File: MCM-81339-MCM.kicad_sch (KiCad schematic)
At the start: 35 parts, among them J3 Conn_02x03_Odd_Even, J5 USB_B_Mini, U5 ESP32-S3-WROOM-2

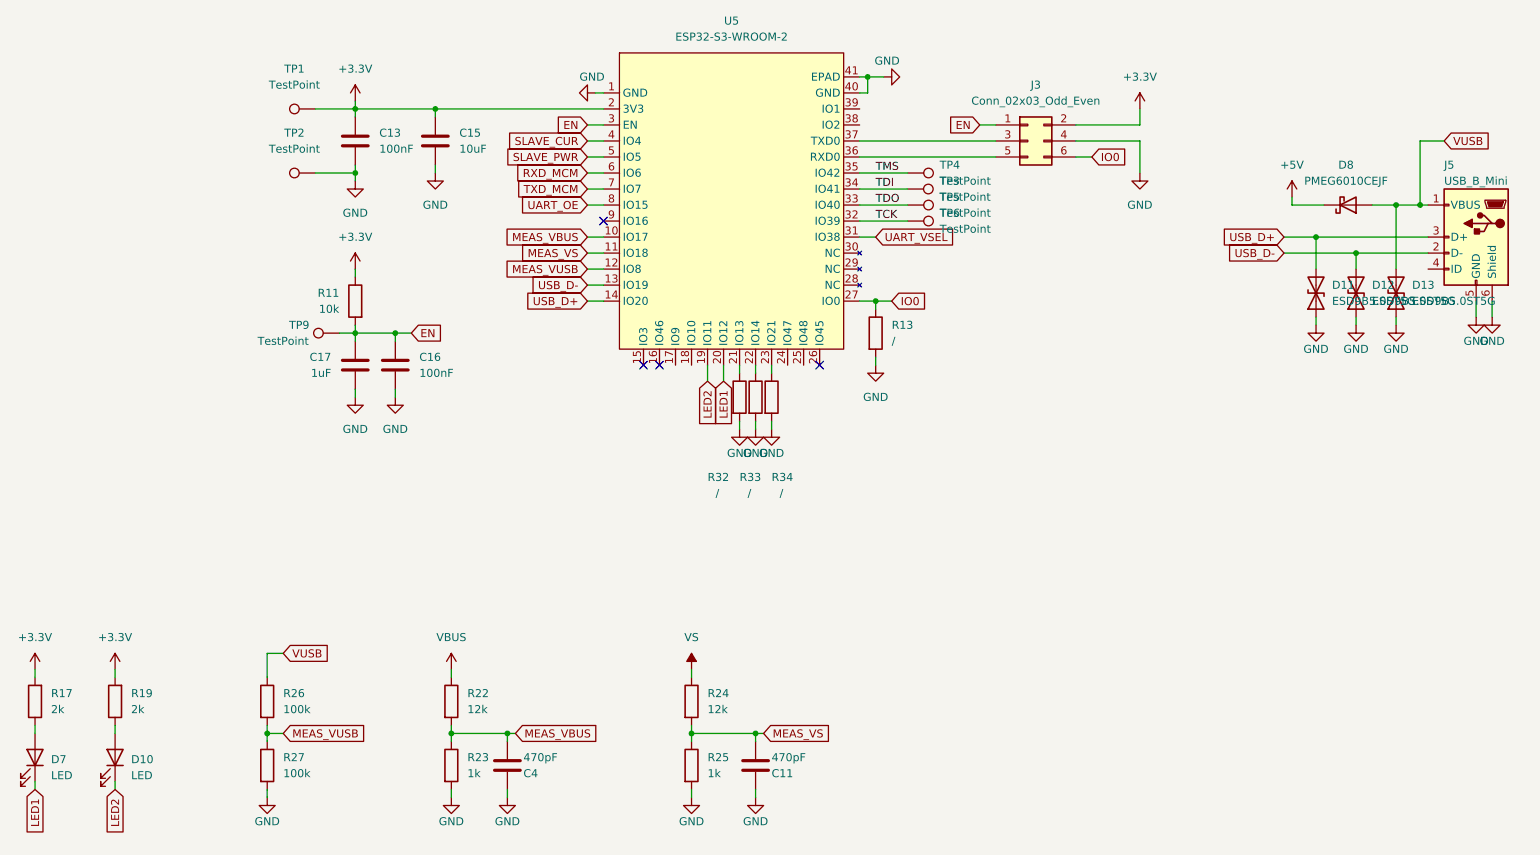
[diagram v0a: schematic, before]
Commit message: add protection on uart, add fab outputs
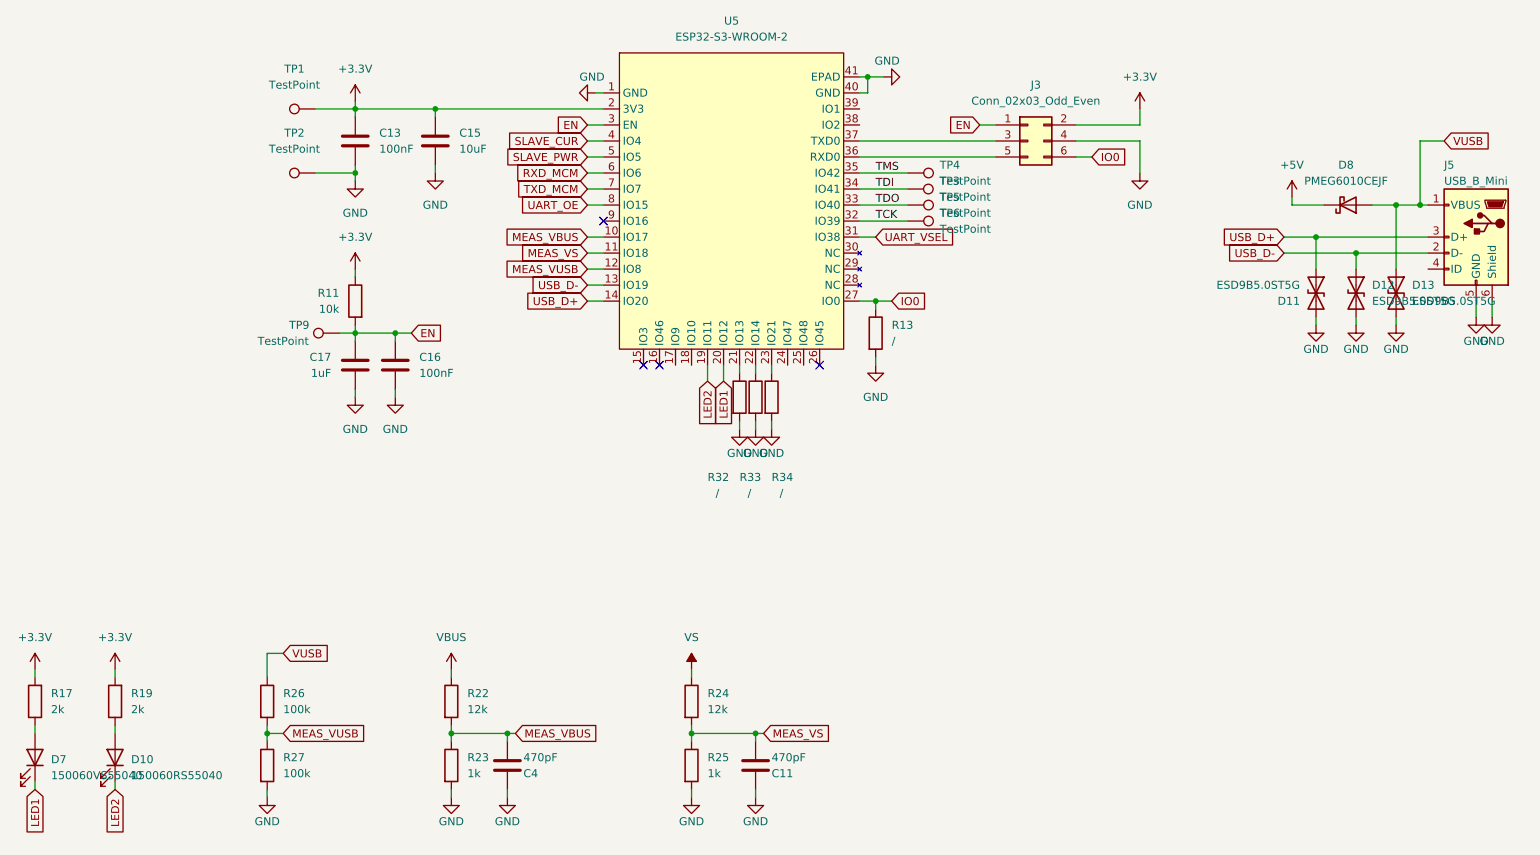
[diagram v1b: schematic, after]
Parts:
- D10: value LED -> 150060RS55040
- D7: value LED -> 150060VS55040
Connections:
- net GND: now also D11.2 (A2), D12.2 (A2), D13.2 (A2); no longer D11.1 (A1), D12.1 (A1), D13.1 (A1)
- net USB_D+: now also D11.1 (A1); no longer D11.2 (A2)
- net USB_D-: now also D12.1 (A1); no longer D12.2 (A2)
- net VUSB: now also D13.1 (A1); no longer D13.2 (A2)
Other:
- moved on the sheet: D11, D12, D13

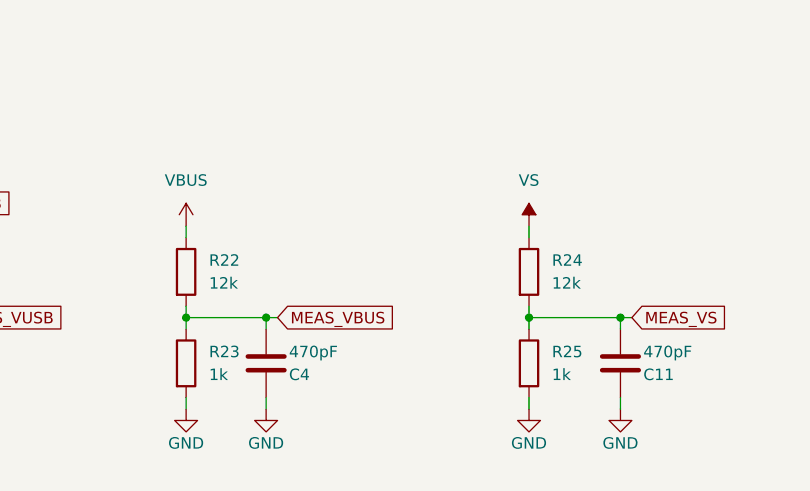
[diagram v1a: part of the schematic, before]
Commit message: R22/R24 to 9k09 for more resolution
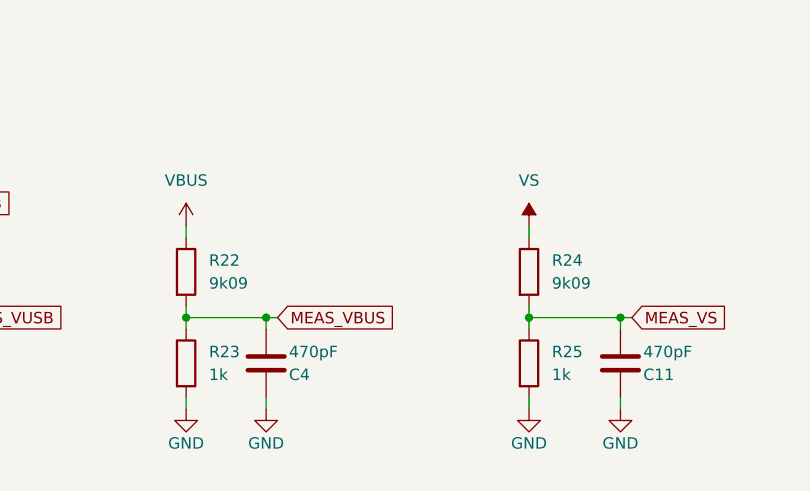
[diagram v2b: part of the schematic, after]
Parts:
- R22, R24: value 12k -> 9k09
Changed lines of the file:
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@@
       (effects (font (size 1.27 1.27)) (justify left))
     )
-    (property "Value" "12k" (id 1) (at 139.7 161.2899 0)
+    (property "Value" "9k09" (id 1) (at 139.7 161.2899 0)
       (effects (font (size 1.27 1.27)) (justify left))
     )
@@
       (effects (font (size 1.27 1.27)) (justify left))
     )
-    (property "Value" "12k" (id 1) (at 101.6 161.2899 0)
+    (property "Value" "9k09" (id 1) (at 101.6 161.2899 0)
       (effects (font (size 1.27 1.27)) (justify left))
     )

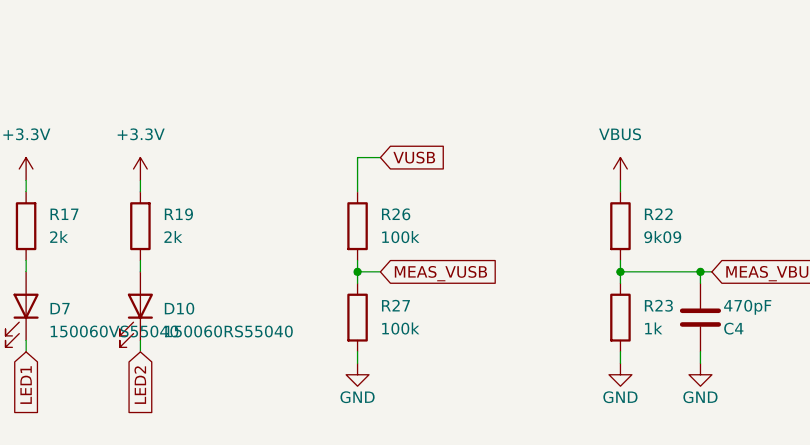
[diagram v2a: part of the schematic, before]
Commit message: update vusb monitor voltage divider
updating vusb voltage divider to get inline with https://docs.espressif.com/projects/esp-idf/en/release-v5.1/esp32s3/api-reference/peripherals/usb_device.html#self-powered-device
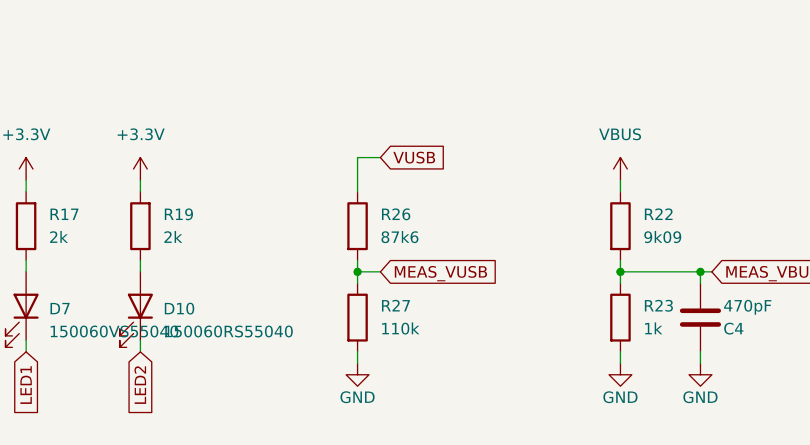
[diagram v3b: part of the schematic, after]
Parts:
- R26: value 100k -> 87k6
- R27: value 100k -> 110k
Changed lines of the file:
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@@
       (effects (font (size 1.27 1.27)) (justify left))
     )
-    (property "Value" "100k" (id 1) (at 72.39 171.4499 0)
+    (property "Value" "110k" (id 1) (at 72.39 171.4499 0)
       (effects (font (size 1.27 1.27)) (justify left))
     )
@@
       (effects (font (size 1.27 1.27)) (justify left))
     )
-    (property "Value" "100k" (id 1) (at 72.39 161.2899 0)
+    (property "Value" "87k6" (id 1) (at 72.39 161.2899 0)
       (effects (font (size 1.27 1.27)) (justify left))
     )
@@
     (pin "1")
   )
+  (sheet_instances
+    (path "/" (page "1"))
+  )
+  (symbol_instances
+    (path "/a512da26-90b0-4ad1-b414-4f5b636f585d"
+      (reference "#PWR01") (unit 1) (value "GND") (footprint "")
+    )
+    (path "/07a4265d-3743-464c-84a0-bda5a34dff7e"
+      (reference "#PWR0130") (unit 1) (value "GND") (footprint "")
+    )
+    (path "/ff3fce4b-50c1-47c2-82ec-c8ec7323b658"
+      (reference "#PWR0131") (unit 1) (value "GND") (footprint "")
+    )
+    (path "/ec2a53fb-5034-4047-8925-cf00391e0117"
+      (reference "#PWR0132") (unit 1) (value "+5V") (footprint "")
+    )
+    (path "/0f37fff6-0fcd-43ec-b64a-f3a6f9cd0d4b"
+      (reference "#PWR0133") (unit 1) (value "GND") (footprint "")
+    )
+    (path "/432211a4-e1f5-498e-969b-56b73638dc5d"
+      (reference "#PWR0134") (unit 1) (value "GND") (footprint "")
+    )
+    (path "/588f378a-ad89-4361-8a6a-c854296bbc92"
+      (reference "#PWR0135") (unit 1) (value "+3.3V") (footprint "")
+    )
+    (path "/6beaa5bd-15ad-4ca4-8935-98a262565292"
+      (reference "#PWR0136") (unit 1) (value "GND") (footprint "")
+    )
+    (path "/728547ca-0b6c-4bab-a1f8-ce21ba9eea66"
+      (reference "#PWR0137") (unit 1) (value "GND") (footprint "")
+    )
+    (path "/7fb277b9-ddb7-4235-894a-7396bcac4ffd"
+      (reference "#PWR0138") (unit 1) (value "+3.3V") (footprint "")
+    )
+    (path "/4e32cc18-1f61-4970-83c3-f8616a2b9f23"
+      (reference "#PWR0139") (unit 1) (value "+3.3V") (footprint "")
+    )
+    (path "/1fadbdd2-16e5-48d6-a35c-2ce721a862e6"
+      (reference "#PWR0140") (unit 1) (value "GND") (footprint "")
+    )
+    (path "/fe850a22-a98d-4d57-9b15-b062912256ed"
+      (reference "#PWR0141") (unit 1) (value "+3.3V") (footprint "")
+    )
+    (path "/6991c44c-e555-42e2-9a9b-08077ea46525"
+      (reference "#PWR0142") (unit 1) (value "GND") (footprint "")
+    )
+    (path "/de0bf633-e9ed-4c7b-a718-e38608204adf"
+      (reference "#PWR0143") (unit 1) (value "GND") (footprint "")
+    )
+    (path "/6c9206fb-eaa0-4897-9024-722230e14d0c"
+      (reference "#PWR0144") (unit 1) (value "+3.3V") (footprint "")
+    )
+    (path "/fe86d367-24e1-43ff-8e0f-5dd999f6717f"
+      (reference "#PWR0145") (unit 1) (value "GND") (footprint "")
+    )
+    (path "/5bccc591-d8c9-4e2e-a1c5-0ad5cafc8380"
+      (reference "#PWR0146") (unit 1) (value "VBUS") (footprint "")
+    )
+    (path "/660f3b83-d37a-4d03-ba2f-abbc4db2de7b"
+      (reference "#PWR0147") (unit 1) (value "GND") (footprint "")
+    )
+    (path "/a89de7a5-c8a0-4697-a76a-8c0a74e23084"
+      (reference "#PWR0148") (unit 1) (value "GND") (footprint "")
+    )
+    (path "/ad614bc0-4d2f-45cc-844b-78fcf25372a1"
+      (reference "#PWR0149") (unit 1) (value "VS") (footprint "")
+    )
+    (path "/cda16e13-e43d-487b-a300-7880bfc03708"
+      (reference "#PWR0150") (unit 1) (value "GND") (footprint "")
+    )
+    (path "/967042b5-4b7a-4c98-a5e8-7efca0b65054"
+      (reference "#PWR0151") (unit 1) (value "GND") (footprint "")
+    )
+    (path "/edc0ee2d-715b-4072-afa2-6cda4d946601"
+      (reference "#PWR0152") (unit 1) (value "GND") (footprint "")
+    )
+    (path "/a611f0d0-59b9-45ae-a121-327fa3788fcb"
+      (reference "#PWR0153") (unit 1) (value "GND") (footprint "")
+    )
+    (path "/3b091975-5427-40db-a3e2-8a25295ebd62"
+      (reference "#PWR0154") (unit 1) (value "GND") (footprint "")
+    )
+    (path "/9feea155-d22d-482d-8bf7-57309a8c16e0"
+      (reference "#PWR0155") (unit 1) (value "GND") (footprint "")
+    )
+    (path "/0395221b-7de6-4cfa-90be-4e99f7c4919e"
+      (reference "#PWR0156") (unit 1) (value "GND") (footprint "")
+    )
+    (path "/bb41d442-d871-48d8-a62c-00607a03e30c"
+      (reference "#PWR0157") (unit 1) (value "GND") (footprint "")
+    )
+    (path "/9e9ae0a4-ec6c-4398-bc24-ad0b433f657c"
+      (reference "C4") (unit 1) (value "470pF") (footprint "Capacitor_SMD:C_0402_1005Metric")
+    )
+    (path "/d545b7e7-927c-4bff-a3ee-bcaec2830f9e"
+      (reference "C11") (unit 1) (value "470pF") (footprint "Capacitor_SMD:C_0402_1005Metric")
+    )
+    (path "/96bdf7e2-fc5f-4bd3-8858-cbb210e0280c"
+      (reference "C13") (unit 1) (value "100nF") (footprint "Capacitor_SMD:C_0402_1005Metric")
+    )
+    (path "/b8721f84-b8d2-4bef-8177-c35bdbd198c0"
+      (reference "C15") (unit 1) (value "10uF") (footprint "Capacitor_SMD:C_1206_3216Metric")
+    )
+    (path "/671a430f-fa11-4bd3-9146-21044a2e710f"
+      (reference "C16") (unit 1) (value "100nF") (footprint "Capacitor_SMD:C_0402_1005Metric")
+    )
+    (path "/85383b02-f665-4bdb-8d30-24ac663a701c"
+      (reference "C17") (unit 1) (value "1uF") (footprint "Capacitor_SMD:C_0402_1005Metric")
+    )
+    (path "/2e5d5d6d-66e5-480c-9d70-d3c142363262"
+      (reference "D7") (unit 1) (value "150060VS55040") (footprint "LED_SMD:LED_0603_1608Metric")
+    )
+    (path "/8345625a-2806-457d-89f5-d8c4b2c12e0f"
+      (reference "D8") (unit 1) (value "PMEG6010CEJF") (footprint "Diode_SMD:D_SOD-323F")
+    )
+    (path "/42fff36f-bacf-4bdf-a68a-1203b70d1064"
+      (reference "D10") (unit 1) (value "150060RS55040") (footprint "LED_SMD:LED_0603_1608Metric")
+    )
+    (path "/990b8ae3-c48c-4659-a142-5c4eb282fb7e"
+      (reference "D11") (unit 1) (value "ESD9B5.0ST5G") (footprint "Diode_SMD:D_SOD-923")
+    )
+    (path "/4efe8f4c-960b-4b4c-b38f-b167b569996e"
+      (reference "D12") (unit 1) (value "ESD9B5.0ST5G") (footprint "Diode_SMD:D_SOD-923")
+    )
+    (path "/7ff5746b-238f-4742-829b-41ca77de7a92"
+      (reference "D13") (unit 1) (value "ESD9B5.0ST5G") (footprint "Diode_SMD:D_SOD-923")
+    )
+    (path "/121686ee-d63e-4f46-b1be-7c3847d981ae"
+      (reference "J3") (unit 1) (value "Conn_02x03_Odd_Even") (footprint "Connector_PinHeader_2.00mm:PinHeader_1x06_P2.00mm_Vertical")
+    )
+    (path "/b16446e8-c716-4508-ac33-6b11e18fa5b2"
+      (reference "J5") (unit 1) (value "USB_B_Mini") (footprint "Connector_USB:USB_Mini-B_Wuerth_65100516121_Horizontal")
+    )
+    (path "/ed070f42-02f9-484f-9141-d09d012dc640"
+      (reference "R11") (unit 1) (value "10k") (footprint "Resistor_SMD:R_0402_1005Metric")
+    )
+    (path "/c123767f-bf20-4e1e-85ce-e10a4bfb3ebe"
+      (reference "R13") (unit 1) (value "/") (footprint "Resistor_SMD:R_0402_1005Metric")
+    )
+    (path "/87df298f-1c8a-49b1-b11f-75bd3967a21b"
+      (reference "R17") (unit 1) (value "2k") (footprint "Resistor_SMD:R_0603_1608Metric")
+    )
+    (path "/57c6c356-e710-48ef-b0b7-fe13fede5acf"
+      (reference "R19") (unit 1) (value "2k") (footprint "Resistor_SMD:R_0603_1608Metric")
+    )
+    (path "/ed7247bd-faeb-4310-9fda-cf37c6b420db"
+      (reference "R22") (unit 1) (value "9k09") (footprint "Resistor_SMD:R_0402_1005Metric")
+    )
+    (path "/d1207b5e-d763-45cd-8fd8-735bcf77ac39"
+      (reference "R23") (unit 1) (value "1k") (footprint "Resistor_SMD:R_0402_1005Metric")
+    )
+    (path "/d225eecb-4d2d-4ebc-bc65-a80f97d891cf"
+      (reference "R24") (unit 1) (value "9k09") (footprint "Resistor_SMD:R_0402_1005Metric")
+    )
+    (path "/94ce5aa1-2dea-40fa-98ce-c2ad0a8a6941"
+      (reference "R25") (unit 1) (value "1k") (footprint "Resistor_SMD:R_0402_1005Metric")
+    )
+    (path "/8cdb8189-4f1a-4c3d-901f-28e5efbf1759"
+      (reference "R26") (unit 1) (value "87k6") (footprint "Resistor_SMD:R_0402_1005Metric")
+    )
+    (path "/2a29fd95-6713-4e44-a108-ed8b91050f57"
+      (reference "R27") (unit 1) (value "110k") (footprint "Resistor_SMD:R_0402_1005Metric")
+    )
+    (path "/ca519420-48db-4eb8-b286-14d6af3b7afd"
+      (reference "R32") (unit 1) (value "/") (footprint "Resistor_SMD:R_0402_1005Metric")
+    )
+    (path "/75c1c33c-38a2-4d9a-9cd0-d1c41eaa0048"
+      (reference "R33") (unit 1) (value "/") (footprint "Resistor_SMD:R_0402_1005Metric")
+    )
+    (path "/db46357a-2240-4019-addb-8038c1793978"
+      (reference "R34") (unit 1) (value "/") (footprint "Resistor_SMD:R_0402_1005Metric")
+    )
+    (path "/6b0c4b71-12b6-4e24-86dd-96d8f7977a05"
+      (reference "TP1") (unit 1) (value "TestPoint") (footprint "TestPoint:TestPoint_Pad_D1.5mm")
+    )
+    (path "/b06610f7-9365-4a5c-abb4-e73298a89c85"
+      (reference "TP2") (unit 1) (value "TestPoint") (footprint "TestPoint:TestPoint_Pad_D1.5mm")
+    )
+    (path "/4b872690-f62c-439c-99d0-8f06392491fc"
+      (reference "TP3") (unit 1) (value "TestPoint") (footprint "TestPoint:TestPoint_Pad_D1.0mm")
+    )
+    (path "/620bb756-65bd-4587-a6f1-0f9aff4bcf5c"
+      (reference "TP4") (unit 1) (value "TestPoint") (footprint "TestPoint:TestPoint_Pad_D1.0mm")
+    )
+    (path "/bbda2527-1e4f-460a-9bea-fb916d574c0e"
+      (reference "TP5") (unit 1) (value "TestPoint") (footprint "TestPoint:TestPoint_Pad_D1.0mm")
+    )
+    (path "/405a1a4f-4845-4340-b7a0-ee4fdc54cf37"
+      (reference "TP6") (unit 1) (value "TestPoint") (footprint "TestPoint:TestPoint_Pad_D1.0mm")
+    )
+    (path "/b59d1dae-f046-4260-abd0-a9a4fe603bfb"
+      (reference "TP9") (unit 1) (value "TestPoint") (footprint "TestPoint:TestPoint_Pad_D1.0mm")
+    )
+    (path "/92da35eb-cd31-4391-be78-b00407543c2b"
+      (reference "U5") (unit 1) (value "ESP32-S3-WROOM-2") (footprint "Melexis:ESP32-S3-WROOM-2")
+    )
+  )
 )

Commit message: use nc pins to route gnd
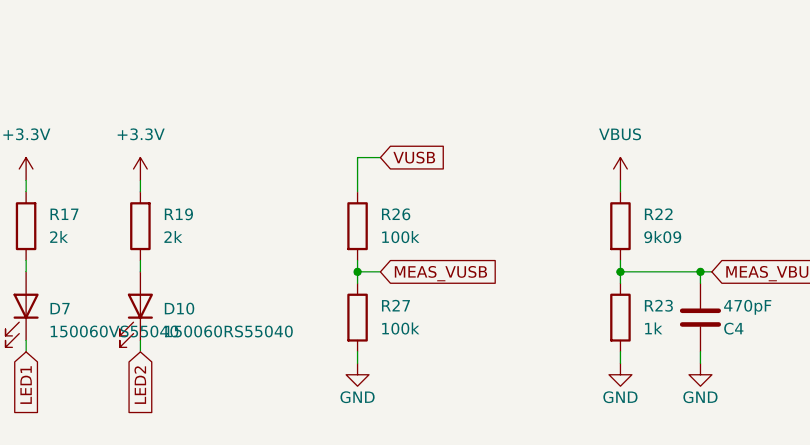
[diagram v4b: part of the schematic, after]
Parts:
- R26: value 87k6 -> 100k
- R27: value 110k -> 100k
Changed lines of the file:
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@@
       (effects (font (size 1.27 1.27)) (justify left))
     )
-    (property "Value" "110k" (id 1) (at 72.39 171.4499 0)
+    (property "Value" "100k" (id 1) (at 72.39 171.4499 0)
       (effects (font (size 1.27 1.27)) (justify left))
     )
@@
       (effects (font (size 1.27 1.27)) (justify left))
     )
-    (property "Value" "87k6" (id 1) (at 72.39 161.2899 0)
-      (effects (font (size 1.27 1.27)) (justify left))
-    )
+    (property "Value" "100k" (id 1) (at 72.39 161.2899 0)
+      (effects (font (size 1.27 1.27)) (justify left))
+    )
